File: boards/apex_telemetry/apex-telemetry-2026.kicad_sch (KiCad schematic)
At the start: 4 parts

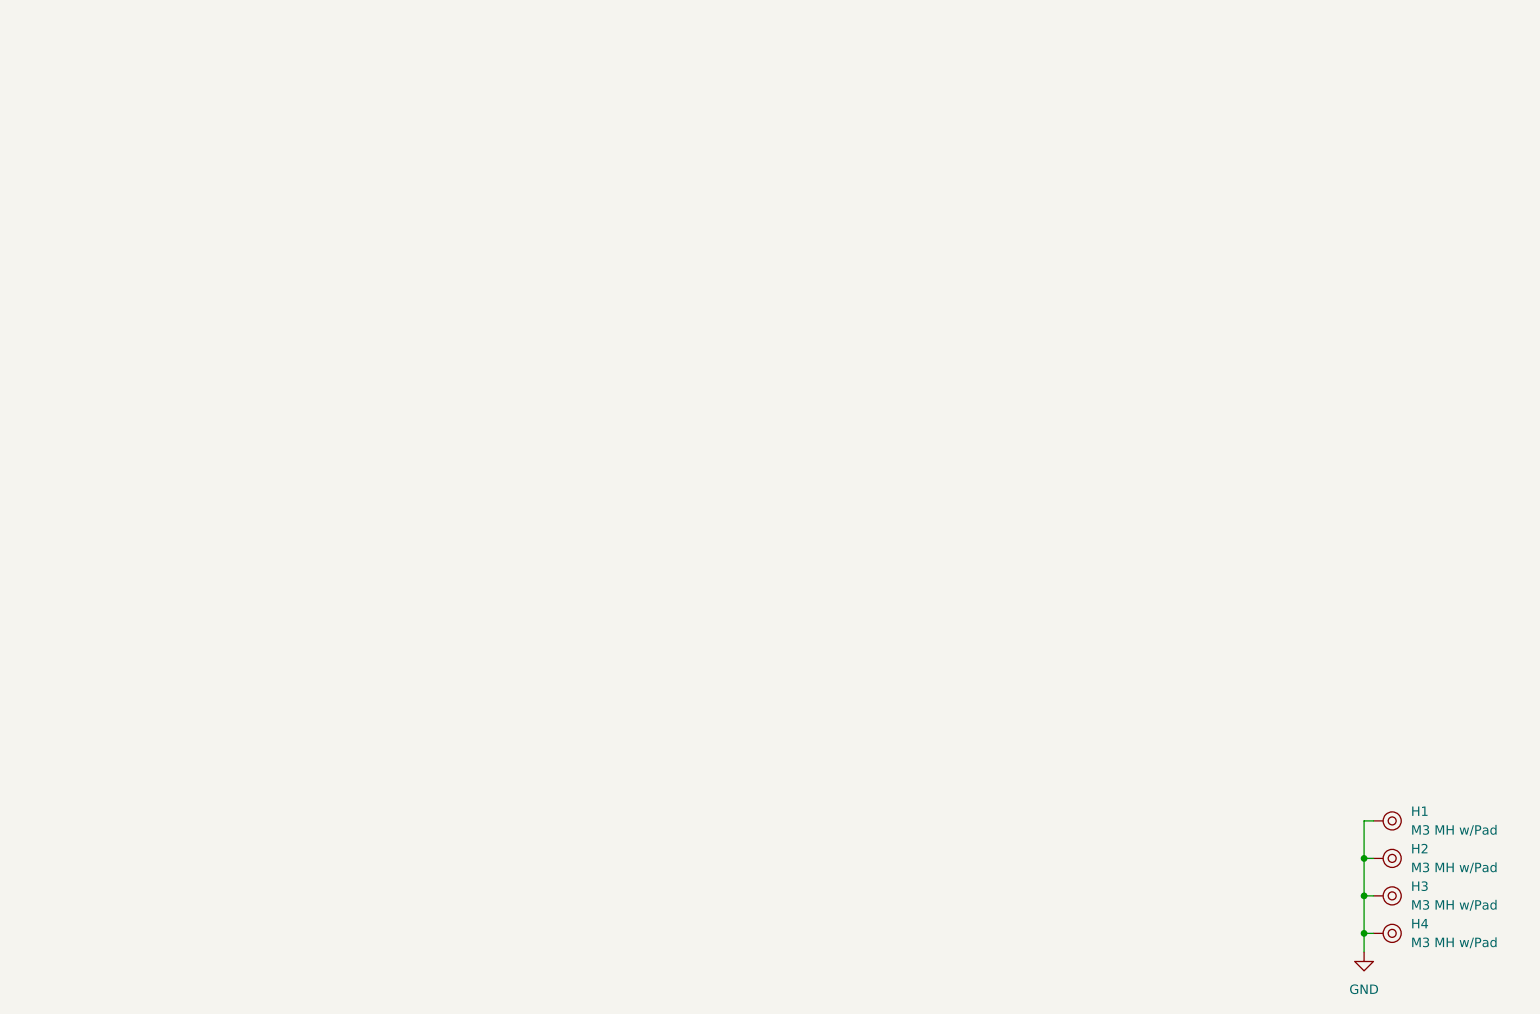
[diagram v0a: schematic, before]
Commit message: Started work on telemetry board schematic
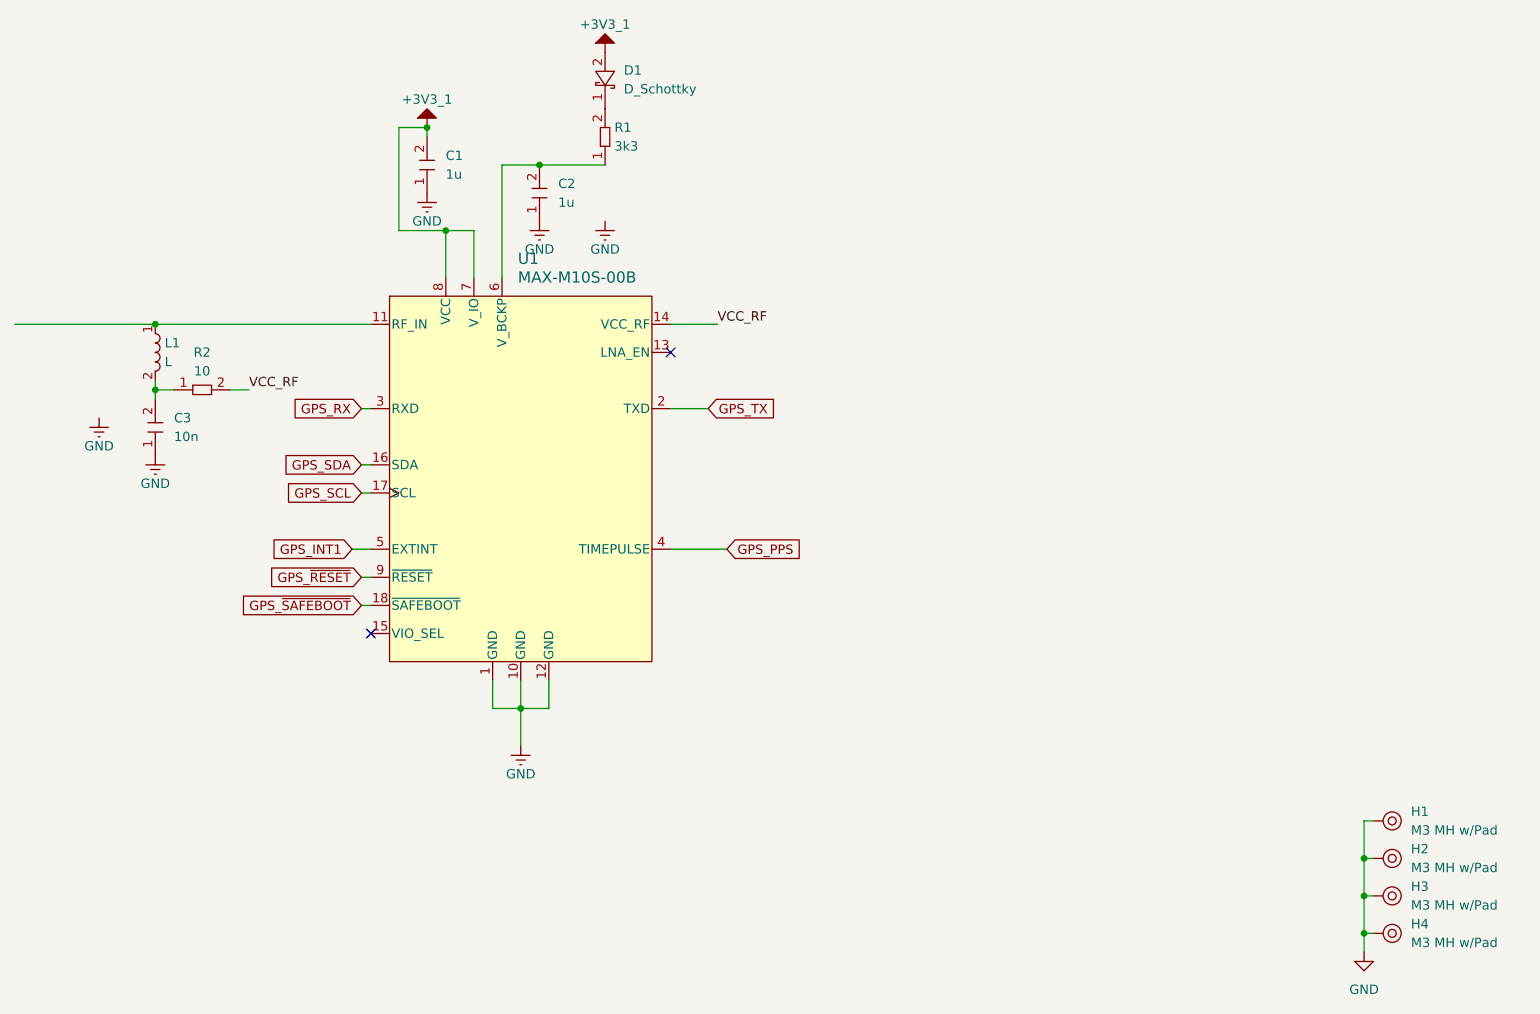
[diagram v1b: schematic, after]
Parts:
- added C1, C2: 1u, symbol APEX_Symbols:C
- added C3: 10n, symbol APEX_Symbols:C
- added D1: D_Schottky, symbol APEX_Symbols:D_Schottky
- added L1: L, symbol APEX_Symbols:L
- added R1: 3k3, symbol APEX_Symbols:R
- added R2: 10, symbol APEX_Symbols:R
- added U1: MAX-M10S-00B, APEX_FOOTPRINTS:MAX-M10S_LCC18_u-blox, symbol APEX_Symbols:MAX-M10S
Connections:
- net GND: now also C1.1, C2.1, C3.1, U1.1 (GND), U1.10 (GND), U1.12 (GND)
- new net: C2.2, R1.1, U1.6 (V_BCKP)
- new net: D1.1 (K), R1.2
- new net: C3.2, L1.2, R2.1
- new net: L1.1, U1.11 (RF_IN)
- new net +3V3_1: C1.2, D1.2 (A), U1.7 (V_IO), U1.8 (VCC)
- new net GPS_INT1: U1.5 (EXTINT)
- new net GPS_PPS: U1.4 (TIMEPULSE)
- new net GPS_RX: U1.3 (RXD)
- new net GPS_SCL: U1.17 (SCL)
- new net GPS_SDA: U1.16 (SDA)
- new net GPS_TX: U1.2 (TXD)
- new net GPS_~{RESET}: U1.9 (~{RESET})
- new net GPS_~{SAFEBOOT}: U1.18 (~{SAFEBOOT})
- new net VCC_RF: R2.2, U1.14 (VCC_RF)
- no-connect marks 0 -> 2
